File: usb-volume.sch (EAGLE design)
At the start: 26 parts, among them SW1 CI-11

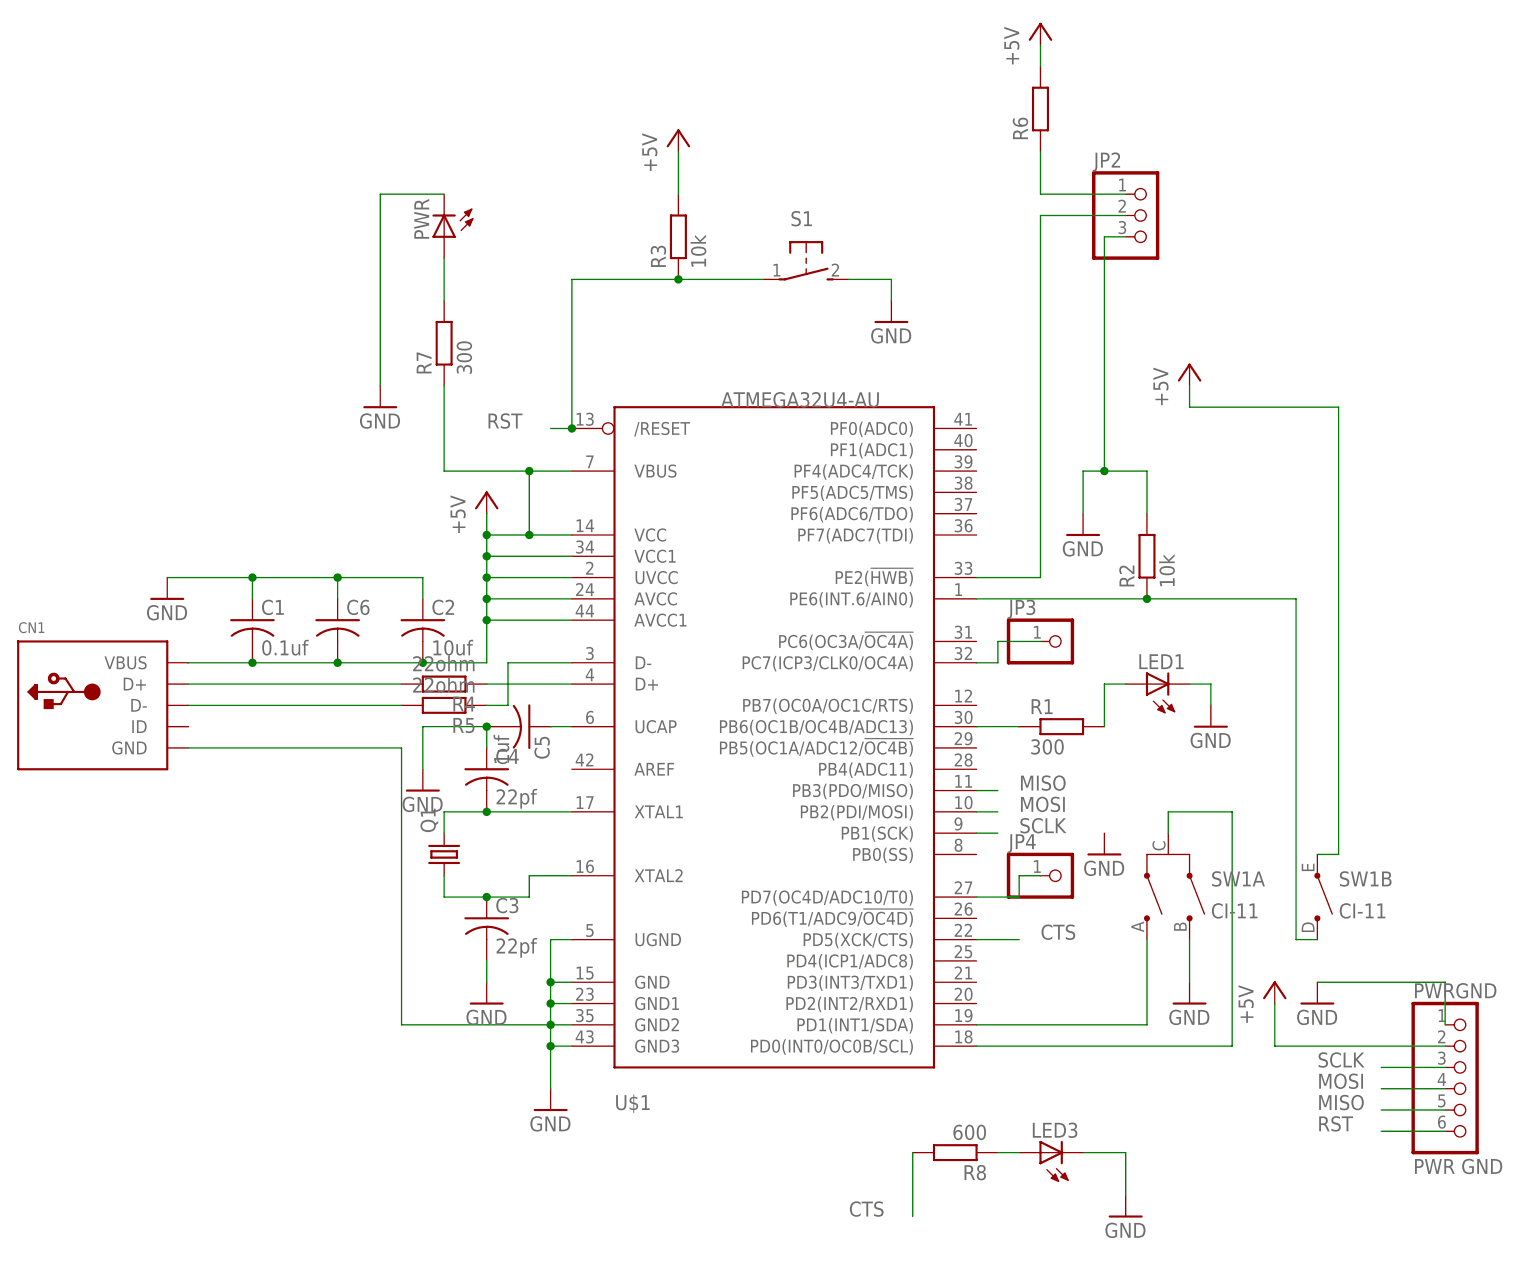
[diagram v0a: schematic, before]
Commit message: updated schematics with values
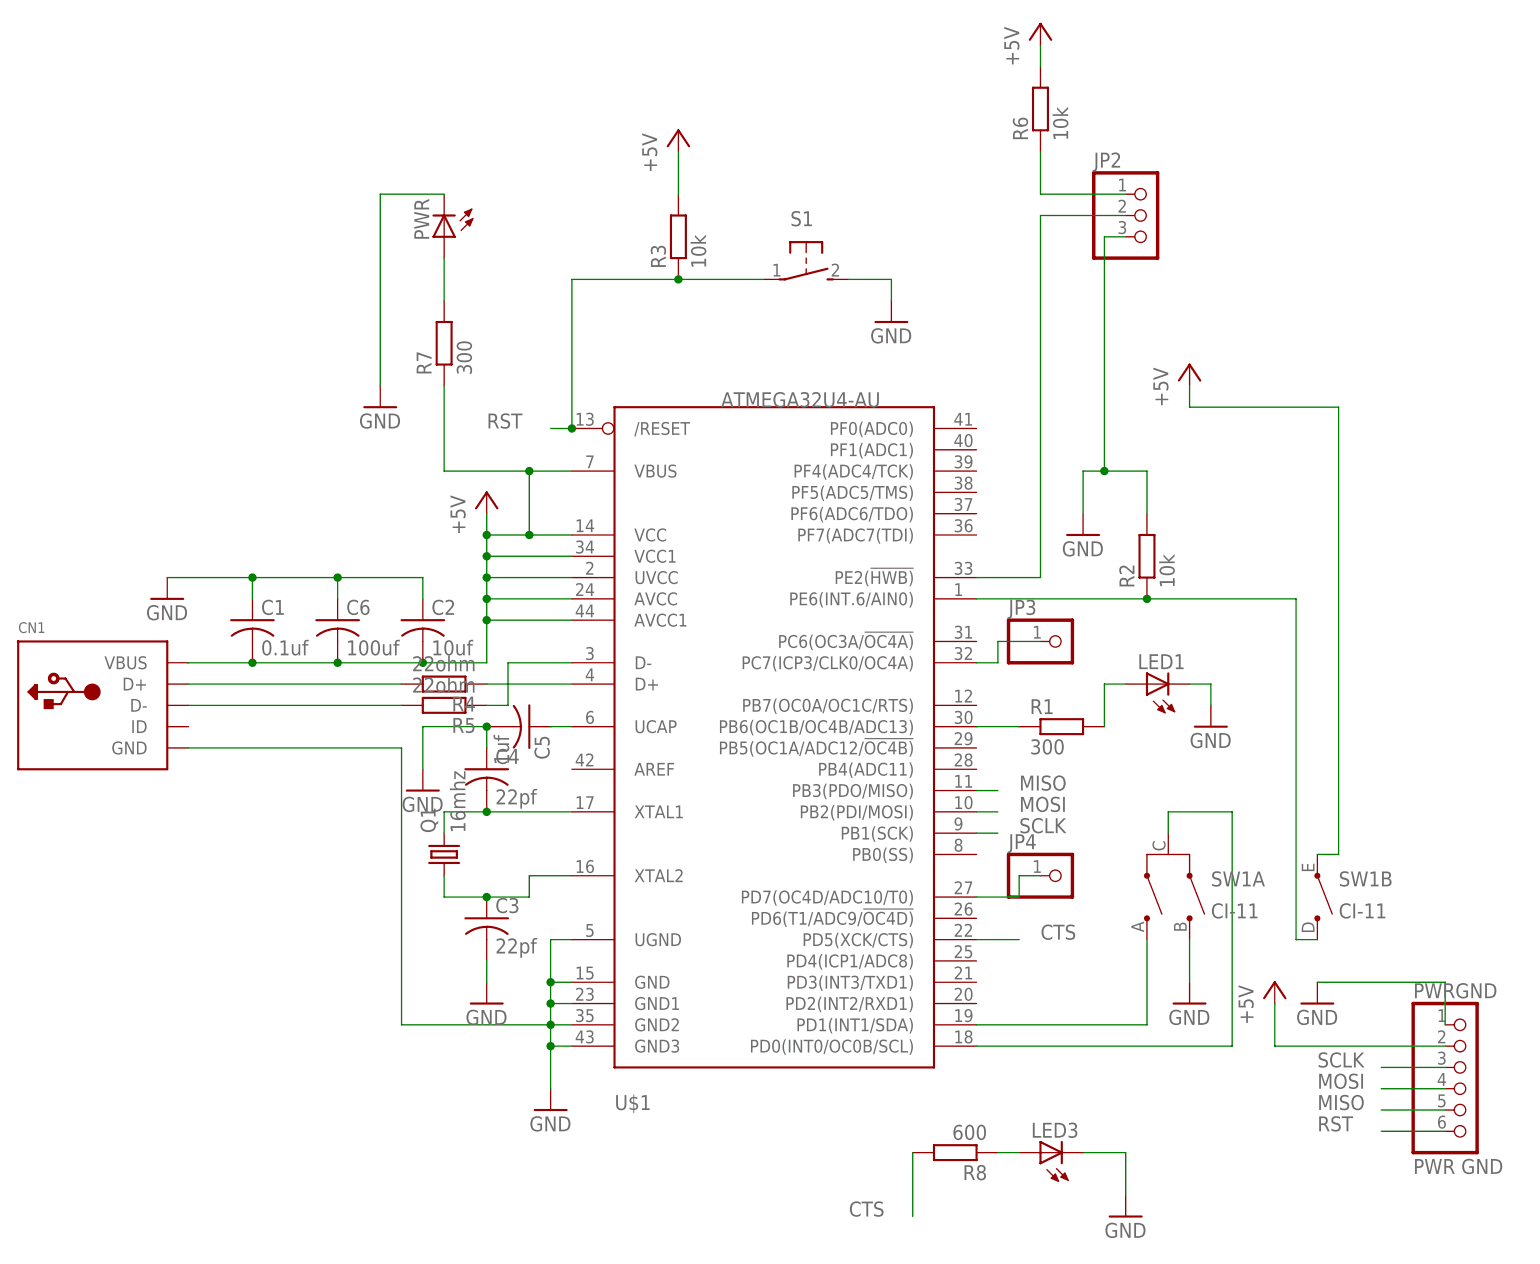
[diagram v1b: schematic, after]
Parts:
- C6: value (none) -> 100uf
- Q1: value (none) -> 16mhz
- R6: value (none) -> 10k
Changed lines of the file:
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@@
 <part name="U$1" library="adafruit" deviceset="ATMEGA32U4" device="-AU"/>
 <part name="SW1" library="piher" deviceset="CI-11" device=""/>
-<part name="GND1" library="supply1" deviceset="GND" device=""/>
 <part name="P+1" library="supply1" deviceset="+5V" device=""/>
 <part name="GND2" library="supply1" deviceset="GND" device=""/>
 <part name="P+2" library="supply1" deviceset="+5V" device=""/>
-<part name="Q1" library="adafruit" deviceset="CRYSTAL" device="HC49S"/>
+<part name="Q1" library="adafruit" deviceset="CRYSTAL" device="HC49S" value="16mhz"/>
 <part name="CN1" library="adafruit" deviceset="USB" device="MINIB"/>
 <part name="LED1" library="adafruit" deviceset="LED" device="5MM"/>
@@
 <part name="R5" library="solar3-1" deviceset="R-EU_" device="R0805" value="22ohm"/>
 <part name="C5" library="adafruit" deviceset="C-US" device="C0805" value="1uf"/>
-<part name="C6" library="adafruit" deviceset="C-US" device="C0805"/>
-<part name="R6" library="solar3-1" deviceset="R-EU_" device="R0805"/>
+<part name="C6" library="adafruit" deviceset="C-US" device="C0805" value="100uf"/>
+<part name="R6" library="solar3-1" deviceset="R-EU_" device="R0805" value="10k"/>
 <part name="P+5" library="supply1" deviceset="+5V" device=""/>
 <part name="JP2" library="adafruit" deviceset="PINHD-1X3" device=""/>
@@
 <instance part="SW1" gate="A" x="114.3" y="38.1"/>
 <instance part="SW1" gate="B" x="132.08" y="38.1"/>
-<instance part="GND1" gate="1" x="106.68" y="43.18"/>
 <instance part="P+1" gate="1" x="116.84" y="101.6"/>
 <instance part="GND2" gate="1" x="40.64" y="12.7"/>
